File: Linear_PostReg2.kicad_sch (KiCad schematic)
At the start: 45 parts, among them Q301 BCP56, Q302 BSS138, Q303 TIP125, Q304 BCP56, U301 TLV4387PWR, U302 LMV331

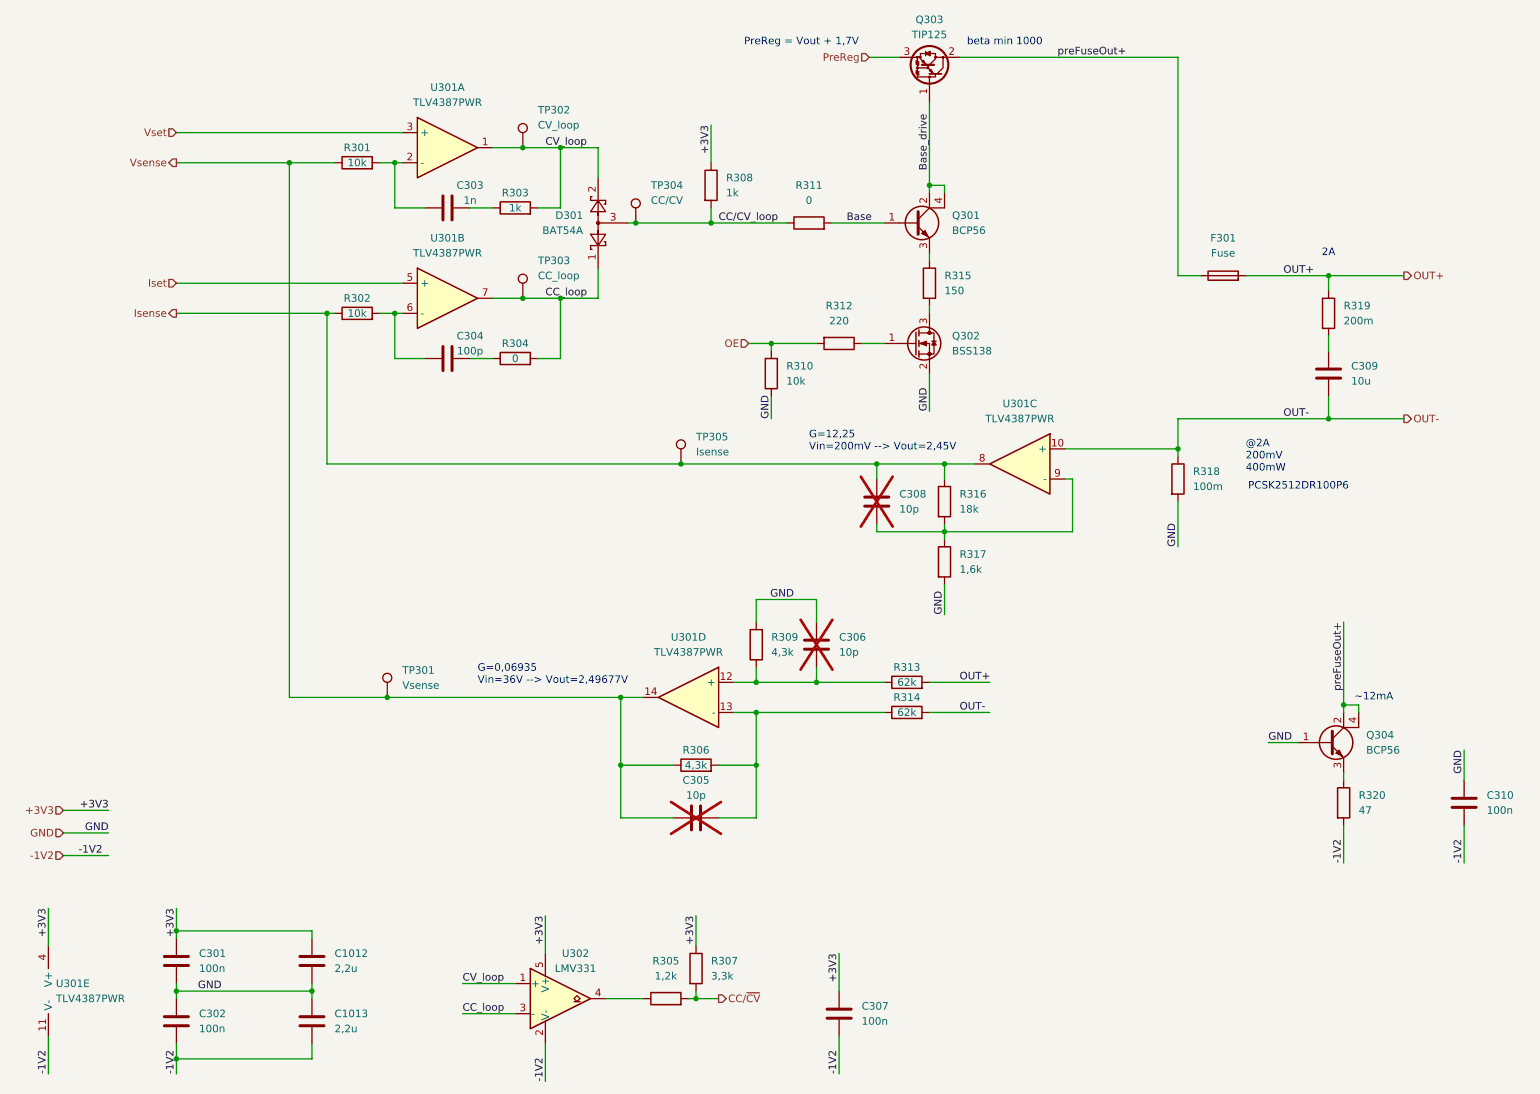
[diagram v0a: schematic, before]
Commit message: added Ch2 and removed global power flags
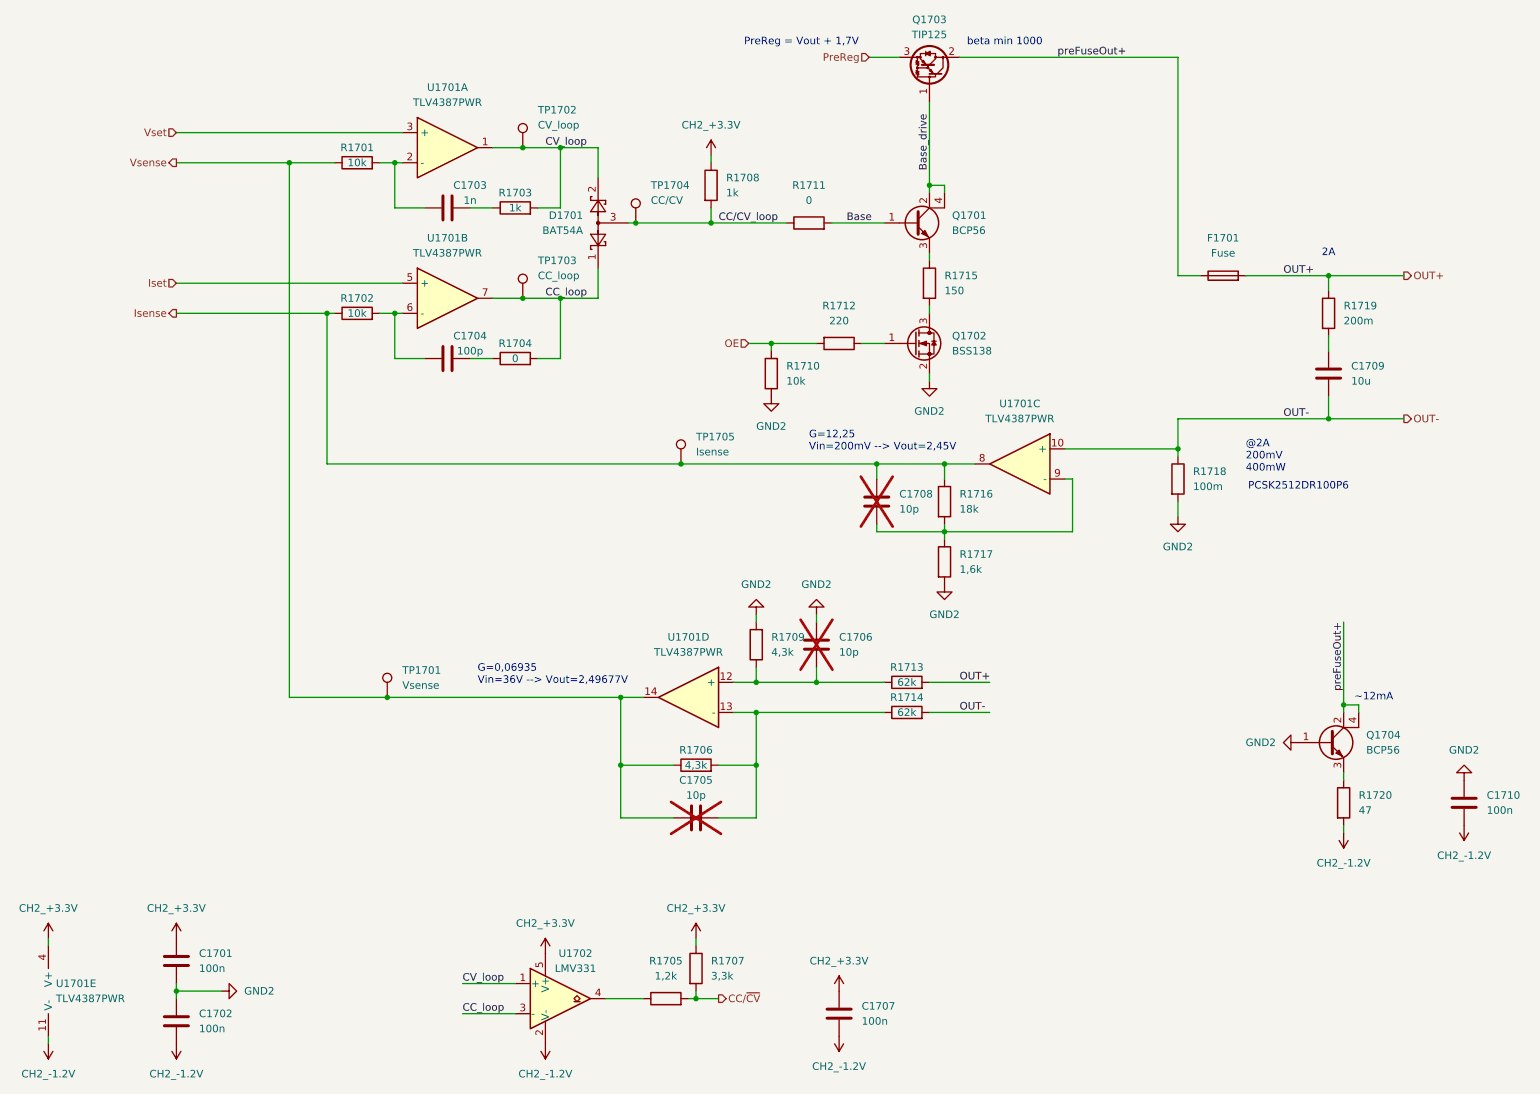
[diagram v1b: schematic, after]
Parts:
- removed C1012, C1013: 2,2u, Capacitor_SMD:C_0603_1608Metric, symbol Device:C
- removed C301, C302, C307, C310: 100n, Capacitor_SMD:C_0603_1608Metric, symbol Device:C
- removed C303: 1n, Capacitor_SMD:C_0603_1608Metric, symbol Device:C
- removed C304: 100p, Capacitor_SMD:C_0603_1608Metric, symbol Device:C
- removed C305, C306, C308: 10p, Capacitor_SMD:C_0603_1608Metric, symbol Device:C
- removed C309: 10u, Capacitor_SMD:C_1206_3216Metric, symbol Device:C
- removed D301: BAT54A, Package_TO_SOT_SMD:SOT-23-3, symbol Diode:BAT54A
- removed F301: Fuse, Fuse:Fuse_1206_3216Metric, symbol Device:Fuse
- removed Q301, Q304: BCP56, Package_TO_SOT_SMD:SOT-223, symbol Transistor_BJT:BCP56
- removed Q302: BSS138, Package_TO_SOT_SMD:SOT-23-3, symbol Transistor_FET:BSS138
- removed Q303: TIP125, Package_TO_SOT_THT:TO-220-3_Horizontal_TabUp, symbol Transistor_BJT:TIP125
- removed R301, R302, R310: 10k, Resistor_SMD:R_0603_1608Metric, symbol Device:R
- removed R303, R308: 1k, Resistor_SMD:R_0603_1608Metric, symbol Device:R
- removed R304, R311: 0, Resistor_SMD:R_0603_1608Metric, symbol Device:R
- removed R305: 1,2k, Resistor_SMD:R_0603_1608Metric, symbol Device:R
- removed R306, R309: 4,3k, Resistor_SMD:R_0603_1608Metric, symbol Device:R
- removed R307: 3,3k, Resistor_SMD:R_0603_1608Metric, symbol Device:R
- removed R312: 220, Resistor_SMD:R_0603_1608Metric, symbol Device:R
- removed R313, R314: 62k, Resistor_SMD:R_0603_1608Metric, symbol Device:R
- removed R315: 150, Resistor_SMD:R_1206_3216Metric, symbol Device:R
- removed R316: 18k, Resistor_SMD:R_0603_1608Metric, symbol Device:R
- removed R317: 1,6k, Resistor_SMD:R_0603_1608Metric, symbol Device:R
- removed R318: 100m, Resistor_SMD:R_2512_6332Metric, symbol Device:R
- removed R319: 200m, Resistor_SMD:R_1206_3216Metric, symbol Device:R
- removed R320: 47, Resistor_SMD:R_0603_1608Metric, symbol Device:R
- removed TP301: Vsense, TestPoint:TestPoint_Pad_D1.0mm, symbol Connector:TestPoint
- removed TP302: CV_loop, TestPoint:TestPoint_Pad_D1.0mm, symbol Connector:TestPoint
- removed TP303: CC_loop, TestPoint:TestPoint_Pad_D1.0mm, symbol Connector:TestPoint
- removed TP304: CC/CV, TestPoint:TestPoint_Pad_D1.0mm, symbol Connector:TestPoint
- removed TP305: Isense, TestPoint:TestPoint_Pad_D1.0mm, symbol Connector:TestPoint
- removed U301: TLV4387PWR, Package_SO:TSSOP-14_4.4x5mm_P0.65mm, symbol Device:Opamp_Quad
- removed U302: LMV331, Package_TO_SOT_SMD:SOT-353_SC-70-5, symbol Comparator:LMV331
- added C1701, C1702, C1707, C1710: 100n, Capacitor_SMD:C_0603_1608Metric, symbol Device:C
- added C1703: 1n, Capacitor_SMD:C_0603_1608Metric, symbol Device:C
- added C1704: 100p, Capacitor_SMD:C_0603_1608Metric, symbol Device:C
- added C1705, C1706, C1708: 10p, Capacitor_SMD:C_0603_1608Metric, symbol Device:C
- added C1709: 10u, Capacitor_SMD:C_1206_3216Metric, symbol Device:C
- added D1701: BAT54A, Package_TO_SOT_SMD:SOT-23-3, symbol Diode:BAT54A
- added F1701: Fuse, Fuse:Fuse_1206_3216Metric, symbol Device:Fuse
- added Q1701, Q1704: BCP56, Package_TO_SOT_SMD:SOT-223, symbol Transistor_BJT:BCP56
- added Q1702: BSS138, Package_TO_SOT_SMD:SOT-23-3, symbol Transistor_FET:BSS138
- added Q1703: TIP125, Package_TO_SOT_THT:TO-220-3_Horizontal_TabUp, symbol Transistor_BJT:TIP125
- added R1701, R1702, R1710: 10k, Resistor_SMD:R_0603_1608Metric, symbol Device:R
- added R1703, R1708: 1k, Resistor_SMD:R_0603_1608Metric, symbol Device:R
- added R1704, R1711: 0, Resistor_SMD:R_0603_1608Metric, symbol Device:R
- added R1705: 1,2k, Resistor_SMD:R_0603_1608Metric, symbol Device:R
- added R1706, R1709: 4,3k, Resistor_SMD:R_0603_1608Metric, symbol Device:R
- added R1707: 3,3k, Resistor_SMD:R_0603_1608Metric, symbol Device:R
- added R1712: 220, Resistor_SMD:R_0603_1608Metric, symbol Device:R
- added R1713, R1714: 62k, Resistor_SMD:R_0603_1608Metric, symbol Device:R
- added R1715: 150, Resistor_SMD:R_1206_3216Metric, symbol Device:R
- added R1716: 18k, Resistor_SMD:R_0603_1608Metric, symbol Device:R
- added R1717: 1,6k, Resistor_SMD:R_0603_1608Metric, symbol Device:R
- added R1718: 100m, Resistor_SMD:R_2512_6332Metric, symbol Device:R
- added R1719: 200m, Resistor_SMD:R_1206_3216Metric, symbol Device:R
- added R1720: 47, Resistor_SMD:R_0603_1608Metric, symbol Device:R
- added TP1701: Vsense, TestPoint:TestPoint_Pad_D1.0mm, symbol Connector:TestPoint
- added TP1702: CV_loop, TestPoint:TestPoint_Pad_D1.0mm, symbol Connector:TestPoint
- added TP1703: CC_loop, TestPoint:TestPoint_Pad_D1.0mm, symbol Connector:TestPoint
- added TP1704: CC/CV, TestPoint:TestPoint_Pad_D1.0mm, symbol Connector:TestPoint
- added TP1705: Isense, TestPoint:TestPoint_Pad_D1.0mm, symbol Connector:TestPoint
- added U1701: TLV4387PWR, Package_SO:TSSOP-14_4.4x5mm_P0.65mm, symbol Device:Opamp_Quad
- added U1702: LMV331, Package_TO_SOT_SMD:SOT-353_SC-70-5, symbol Comparator:LMV331
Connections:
- net Base: now also Q1701.1 (B), R1711.2
- net Base_drive: now also Q1701.2 (C), Q1701.4 (C), Q1703.1 (B)
- net CC_loop: now also D1701.1, R1704.2, TP1703.1, U1701.7, U1702.3 (-)
- net CC/CV_loop: now also D1701.3, R1708.2, R1711.1, TP1704.1
- net CC/~{CV}: now also R1705.2, R1707.2
- net CV_loop: now also D1701.2, R1703.2, TP1702.1, U1701.1, U1702.1 (+)
- net Isense: now also C1708.1, R1702.1, R1716.1, TP1705.1, U1701.8
- net Iset: now also U1701.5 (+)
- net OE: now also R1710.2, R1712.2
- net OUT+: now also F1701.2, R1713.2, R1719.1
- net OUT-: now also C1709.2, R1714.2, R1718.1, U1701.10 (+)
- net PreReg: now also Q1703.3 (E)
- net Vsense: now also C1705.1, R1701.1, R1706.1, TP1701.1, U1701.14
- net Vset: now also U1701.3 (+)
- net preFuseOut+: now also F1701.1, Q1703.2 (C), Q1704.2 (C), Q1704.4 (C)
- new net: C1703.2, R1703.1
- new net: C1704.1, R1702.2, U1701.6 (-)
- new net: C1705.2, R1706.2, R1714.1, U1701.13 (-)
- new net: C1703.1, R1701.2, U1701.2 (-)
- new net: Q1702.1 (G), R1712.1
- new net: C1706.2, R1709.1, R1713.1, U1701.12 (+)
- new net: R1705.1, U1702.4
- new net: C1704.2, R1704.1
- new net: Q1704.3 (E), R1720.1
- new net: C1709.1, R1719.2
- new net: C1708.2, R1716.2, R1717.1, U1701.9 (-)
- new net: Q1701.3 (E), R1715.1
- new net: Q1702.3 (D), R1715.2
- new net CH2_+3.3V: C1701.1, C1707.1, R1707.1, R1708.1, U1701.4 (V+), U1702.5 (V+)
- new net CH2_-1.2V: C1702.2, C1707.2, C1710.2, R1720.2, U1701.11 (V-), U1702.2 (V-)
- new net GND2: C1701.2, C1702.1, C1706.1, C1710.1, Q1702.2 (S), Q1704.1 (B), R1709.2, R1710.1, R1717.2, R1718.2
